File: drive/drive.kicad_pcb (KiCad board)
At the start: 2 copper layers, 50 x 31 mm, 36 parts, among them J1 MOTOR, J2 28V~~, J3 CAN, J4 AVR-ISP-6, Q2 2N7002, Q3 BTA06-600TW, U1 LM317LI, U2 MCP2551-I-SN, U3 ATmega32M1-AU, Y1 16MHz

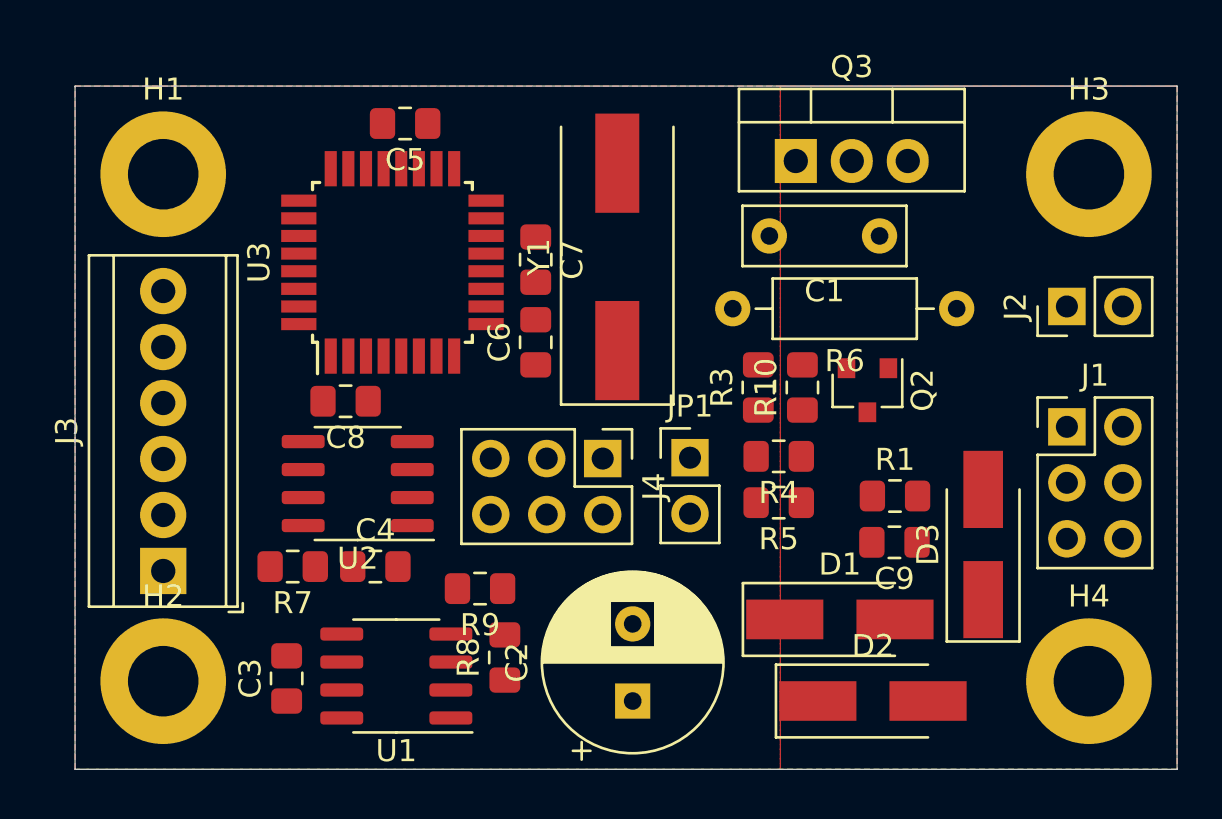
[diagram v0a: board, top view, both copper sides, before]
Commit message: drive: optimized routing and power plance placement
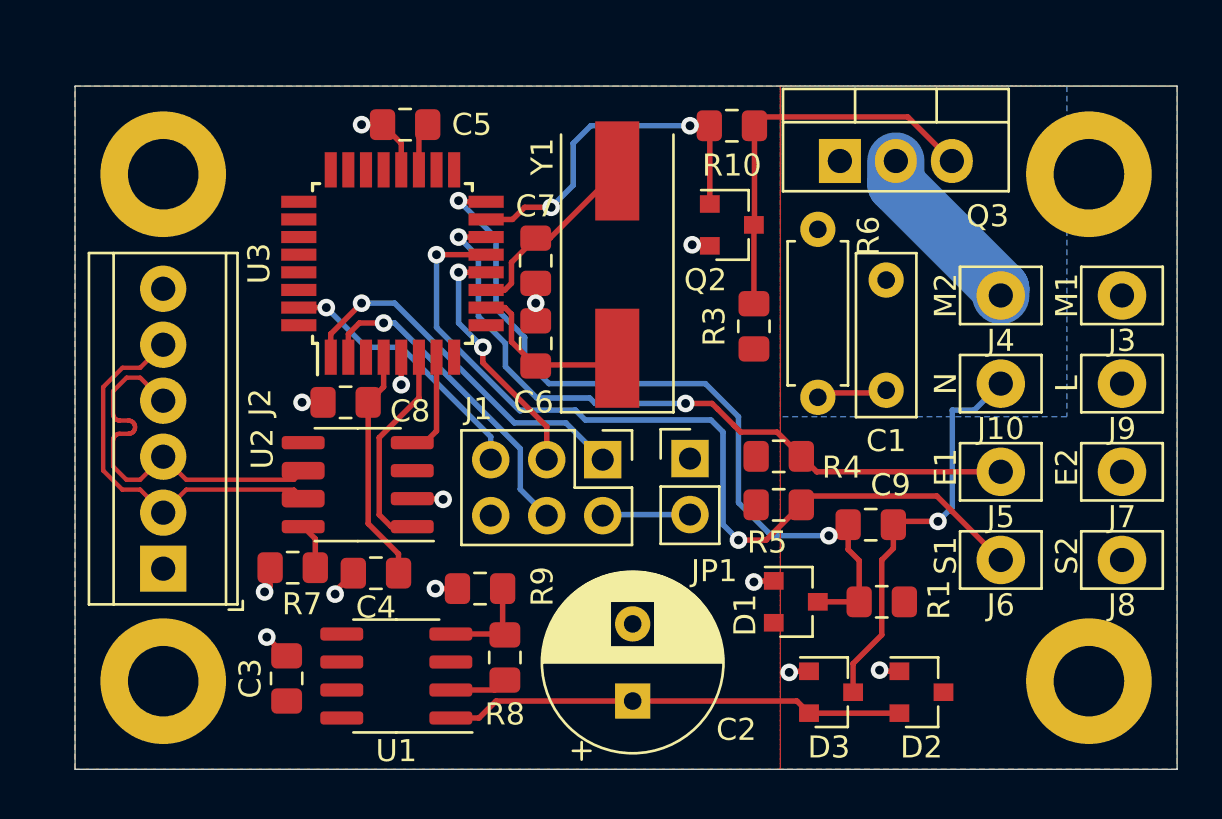
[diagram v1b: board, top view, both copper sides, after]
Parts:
- removed the J1 at (195.0, 85.5)
- added J10: 28VAC, Connector_Pin:Pin_D1.1mm_L10.2mm_W3.5mm_Flat, F.Cu at (192.0, 83.5)
- added J4: MOTOR2, Connector_Pin:Pin_D1.1mm_L10.2mm_W3.5mm_Flat, F.Cu at (192.0, 79.5)
- added J5: EMPTY1, Connector_Pin:Pin_D1.1mm_L10.2mm_W3.5mm_Flat, F.Cu at (192.0, 87.5)
- added J6: STOP1, Connector_Pin:Pin_D1.1mm_L10.2mm_W3.5mm_Flat, F.Cu at (192.0, 91.5)
- added J7: EMPTY2, Connector_Pin:Pin_D1.1mm_L10.2mm_W3.5mm_Flat, F.Cu at (197.5, 87.5)
- added J8: STOP2, Connector_Pin:Pin_D1.1mm_L10.2mm_W3.5mm_Flat, F.Cu at (197.5, 91.5)
- added J9: 28VAC, Connector_Pin:Pin_D1.1mm_L10.2mm_W3.5mm_Flat, F.Cu at (197.5, 83.5)
- D1, D2, D3: value SS14 -> BAS40-04; footprint Diode_SMD:D_SMA_Handsoldering -> Package_TO_SOT_SMD:SOT-23
- J2: value 28V~~ -> CAN; footprint Connector_PinHeader_2.54mm:PinHeader_1x02_P2.54mm_Vertical -> TerminalBlock_TE-Connectivity:TerminalBlock_TE_282834-6_1x06_P2.54mm_Horizontal
- J3: value CAN -> MOTOR1; footprint TerminalBlock_TE-Connectivity:TerminalBlock_TE_282834-6_1x06_P2.54mm_Horizontal -> Connector_Pin:Pin_D1.1mm_L10.2mm_W3.5mm_Flat
- R6: footprint Resistor_THT:R_Axial_DIN0207_L6.3mm_D2.5mm_P10.16mm_Horizontal -> Resistor_THT:R_Axial_DIN0207_L6.3mm_D2.5mm_P7.62mm_Horizontal
- moved J3 45.3 mm to (197.5, 79.5), turned to 0 degrees
- moved J2 42.7 mm to (154.0, 91.9)
- moved R10 12.3 mm to (179.8, 71.8), turned to 180 degrees
- moved Q2 9.70 mm to (179.8, 76.3), turned to 0 degrees
- moved D3 9.62 mm to (184.3, 97.5), turned to 0 degrees
- moved R6 7.26 mm to (183.7, 76.5), turned to 270 degrees
- moved C1 7.01 mm to (186.8, 83.8), turned to 90 degrees
- moved R1 4.84 mm to (186.6, 93.4), turned to 180 degrees
- moved R3 2.78 mm to (180.8, 80.9), turned to 270 degrees
- moved D2 2.24 mm to (188.4, 97.5)
- moved D1 2.15 mm to (182.7, 93.4)
- moved Q3 2.00 mm to (184.7, 73.4)
- moved C9 1.34 mm to (186.1, 89.9), turned to 0 degrees
- moved Y1 0.35 mm to (174.6, 78.1)
- moved C4 0.30 mm to (163.7, 92.1), turned to 180 degrees
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- renumbered J4 to J1
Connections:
- C1 pad 2: GND -> NEUT
- C9 pad 2: GND -> NEUT
- D1 pad 1: +5V -> GND
- D1 pad 2: /ZERO -> +5V
- D2 pad 1: Net-(C2-Pad1) -> GND
- D2 pad 2: LINE -> Net-(C2-Pad1)
- D3 pad 1: /ZERO -> GND
- D3 pad 2: GND -> Net-(C2-Pad1)
- J2 pad 1: LINE -> GND
- J2 pad 2: GND -> /CAN_P
- J3 pad 1: GND -> LINE
- Q3 pad 1: GND -> NEUT
- U3 pad 13: (no net) -> /STOP1
- U3 pad 14: (no net) -> /EMPTY1
- U3 pad 15: (no net) -> /TRIGGER
- U3 pad 16: /STOP1 -> /ZERO
- U3 pad 23: /EMPTY1 -> (no net)
- U3 pad 24: /ZERO -> (no net)
- U3 pad 28: /TRIGGER -> (no net)
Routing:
- net /STOP1: track 0.00 -> 39.7 mm, vias 0 -> 2
- net /ZERO: track 0.00 -> 35.8 mm, vias 0 -> 2
- net /EMPTY1: track 0.00 -> 32.5 mm, vias 0 -> 2
- net Net-(C2-Pad1): track 0.00 -> 20.9 mm
- net NEUT: track 0.00 -> 18.5 mm, vias 0 -> 1
- net Net-(Q2-Pad3): track 0.00 -> 18.0 mm
- net /CAN_P: track 0.00 -> 17.8 mm
- net /CAN_N: track 0.00 -> 17.8 mm
- net GND: track 0.00 -> 17.0 mm, vias 0 -> 13
- net /MISO: track 0.00 -> 16.9 mm, vias 0 -> 1
- net /TRIGGER: track 0.00 -> 16.6 mm, vias 0 -> 2
- net +5V: track 0.00 -> 15.5 mm
- net /MOSI: track 0.00 -> 15.0 mm, vias 0 -> 1
- net /~RESET: track 0.00 -> 12.2 mm, vias 0 -> 1
- net /SCK: track 0.00 -> 11.4 mm, vias 0 -> 2
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- added copper zone on B.Cu, net NEUT
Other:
- net class CAN added: clearance 0.2, trace_width 0.2, via_dia 0.8, via_drill 0.4
- net class Power added: clearance 0.2, trace_width 2.6, via_dia 3, via_drill 1.2
- rule pad_to_mask_clearance: 0.05 -> 0
- board text added: "E1"
- board text added: "E2"
- board text added: "L"
- board text added: "M1"
- board text added: "M2"
- board text added: "N"
- board text added: "S1"
- board text added: "S2"

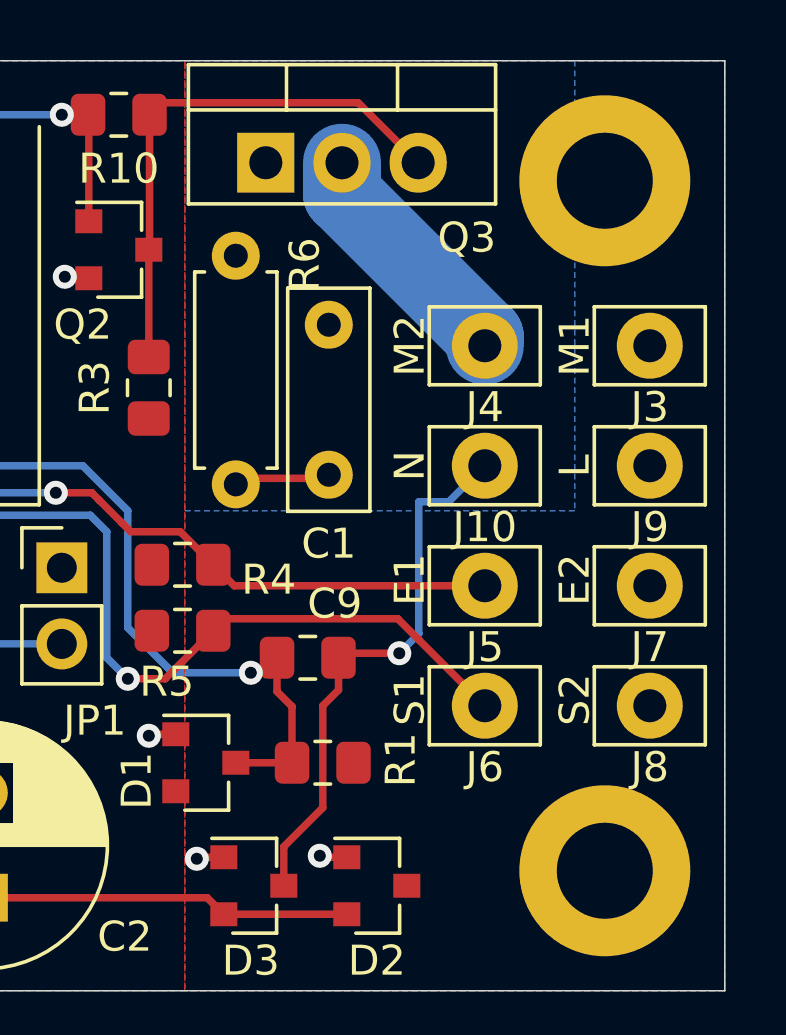
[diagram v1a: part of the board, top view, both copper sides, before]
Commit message: Replace power pins with mini-fit jr
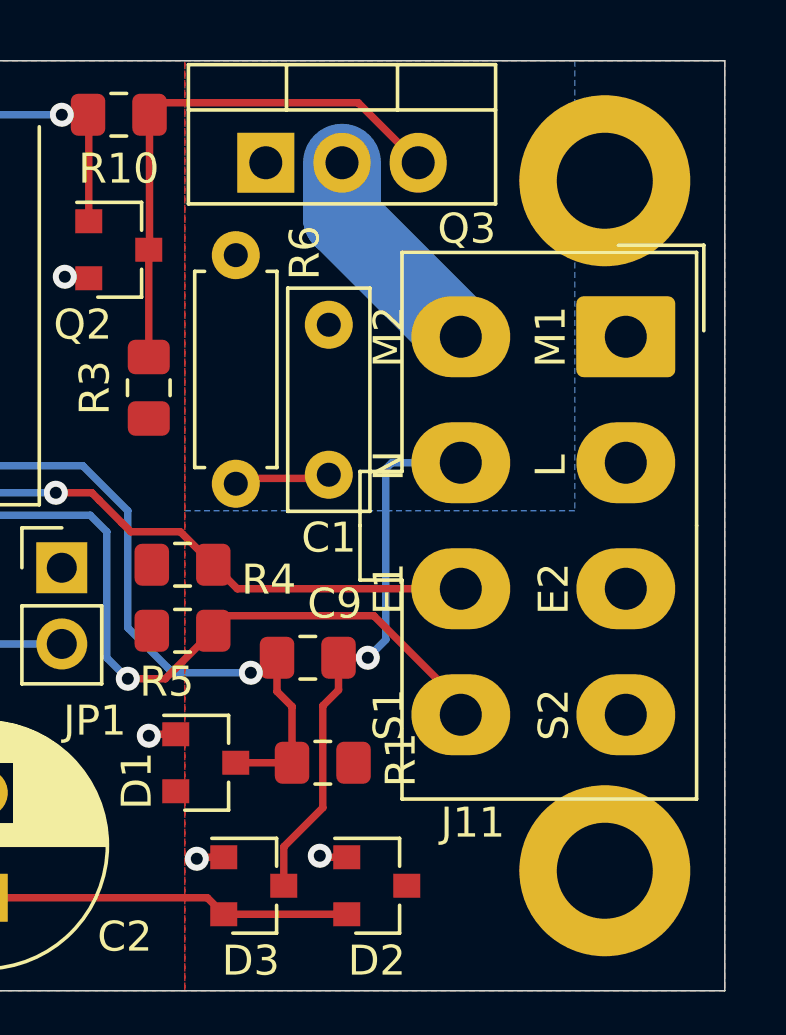
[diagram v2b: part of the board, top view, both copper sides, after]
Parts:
- removed J10, J9: 28VAC, Connector_Pin:Pin_D1.1mm_L10.2mm_W3.5mm_Flat
- removed J3: MOTOR1, Connector_Pin:Pin_D1.1mm_L10.2mm_W3.5mm_Flat
- removed J4: MOTOR2, Connector_Pin:Pin_D1.1mm_L10.2mm_W3.5mm_Flat
- removed J5: EMPTY1, Connector_Pin:Pin_D1.1mm_L10.2mm_W3.5mm_Flat
- removed J6: STOP1, Connector_Pin:Pin_D1.1mm_L10.2mm_W3.5mm_Flat
- removed J7: EMPTY2, Connector_Pin:Pin_D1.1mm_L10.2mm_W3.5mm_Flat
- removed J8: STOP2, Connector_Pin:Pin_D1.1mm_L10.2mm_W3.5mm_Flat
- added J11: Power, Connector_Molex:Molex_Mini-Fit_Jr_5566-08A_2x04_P4.20mm_Vertical, F.Cu at (196.7, 79.2)
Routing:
- net /EMPTY1: track 32.5 -> 31.7 mm
- net /MOTOR2: track 8.07 -> 7.44 mm

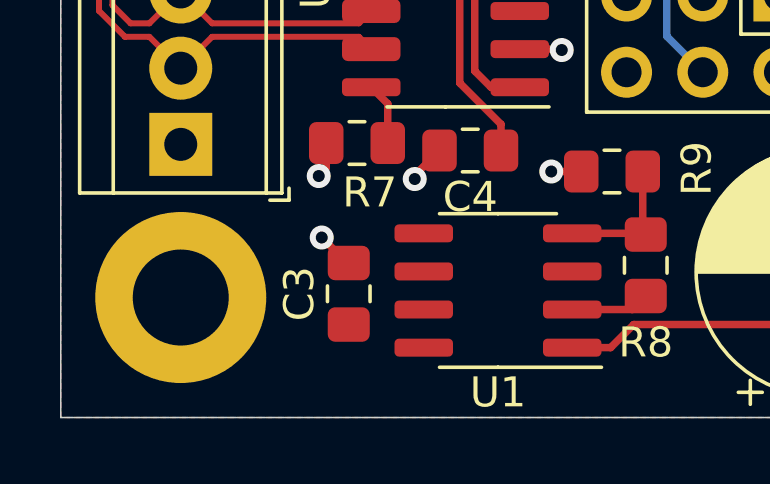
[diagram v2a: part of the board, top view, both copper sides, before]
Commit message: Replaced BAS-40 with BAS-70 to avoid peak-peak overvoltage
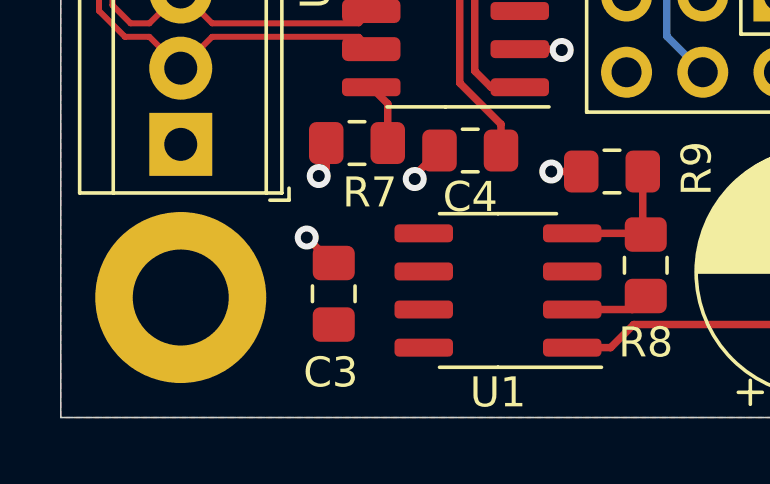
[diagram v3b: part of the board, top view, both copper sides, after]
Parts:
- moved C3 0.50 mm to (159.1, 96.9)
